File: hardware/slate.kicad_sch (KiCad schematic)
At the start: 0 parts

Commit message: DDR3 RAM symbol
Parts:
- added U1: A33, slate-lib:TFBGA-282_14x14mm_Layout17x17_P0.8mm, symbol slate-lib:A33
- added U2: H5TQ4G63EFR, Package_BGA:FBGA-96_7.5x13mm_Layout9x16_P0.8mm, symbol slate-lib:H5TQ4G63EFR
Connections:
- new net: U2.J1 (NC), U2.J9 (NC), U2.L1 (NC), U2.L9 (NC), U2.M7 (NC)
- new net GND: U1.F10 (GND), U1.F8 (GND), U1.F9 (GND), U1.G10 (GND), U1.G11 (GND), U1.G7 (GND), U1.G8 (GND), U1.G9 (GND), U1.H10 (GND), U1.H11 (GND), U1.H12 (GND), U1.H13 (AGND), U1.H7 (GND), U1.H8 (GND), U1.H9 (GND), U1.J10 (GND), U1.J11 (GND), U1.J12 (GND), U1.J7 (GND), U1.J8 (GND), U1.J9 (GND), U1.K10 (GND), U1.K11 (GND), U1.K12 (GND), U1.K7 (GND), U1.K8 (GND), U1.K9 (GND), U1.L10 (GND), U1.L11 (GND), U1.L8 (GND), U1.L9 (GND), U1.M10 (GND), U1.M9 (GND), U1.N4 (GND), U2.A9 (VSS), U2.B1 (VSSQ), U2.B3 (VSS), U2.B9 (VSSQ), U2.D1 (VSSQ), U2.D8 (VSSQ), U2.E1 (VSS), U2.E2 (VSSQ), U2.E8 (VSSQ), U2.F9 (VSSQ), U2.G1 (VSSQ), U2.G8 (VSS), U2.G9 (VSSQ), U2.J2 (VSS), U2.J8 (VSS), U2.M1 (VSS), U2.M9 (VSS), U2.P1 (VSS), U2.P9 (VSS), U2.T1 (VSS), U2.T9 (VSS)
- new net VCC-DRAM: U1.H5 (VCC-DRAM), U1.H6 (VCC-DRAM), U1.J5 (VCC-DRAM), U1.J6 (VCC-DRAM), U1.K5 (VCC-DRAM), U1.L5 (VCC-DRAM)
- new net VCC-IO: U1.E11 (VCC-IO), U1.E12 (VCC-IO), U1.F11 (VCC-IO), U1.F12 (VCC-IO), U1.G12 (VCC-IO)
- new net VCC-PD: U1.M11 (VCC-PD), U1.N11 (VCC-PD)
- new net VDD: U2.B2 (VDD), U2.D9 (VDD), U2.G7 (VDD), U2.K2 (VDD), U2.K8 (VDD), U2.N1 (VDD), U2.N9 (VDD), U2.R1 (VDD), U2.R9 (VDD)
- new net VDD-CPU: U1.E5 (VDD-CPU), U1.E6 (VDD-CPU), U1.E7 (VDD-CPU), U1.F5 (VDD-CPU), U1.F6 (VDD-CPU), U1.F7 (VDD-CPU), U1.G5 (VDD-CPU), U1.G6 (VDD-CPU)
- new net VDD-SYS: U1.E10 (VDD-SYS), U1.E8 (VDD-SYS), U1.E9 (VDD-SYS), U1.K6 (VDD-SYS), U1.L6 (VDD-SYS), U1.M6 (VDD-SYS), U1.M7 (VDD-SYS), U1.N10 (VDD-SYS), U1.N8 (VDD-SYS), U1.N9 (VDD-SYS)
- new net VDDQ: U2.A1 (VDDQ), U2.A8 (VDDQ), U2.C1 (VDDQ), U2.C9 (VDDQ), U2.D2 (VDDQ), U2.E9 (VDDQ), U2.F1 (VDDQ), U2.H2 (VDDQ), U2.H9 (VDDQ)

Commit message: Update
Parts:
- removed U1: A33, slate-lib:TFBGA-282_14x14mm_Layout17x17_P0.8mm, symbol slate-lib:A33
- removed U2: H5TQ4G63EFR, Package_BGA:FBGA-96_7.5x13mm_Layout9x16_P0.8mm, symbol slate-lib:H5TQ4G63EFR
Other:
- added sheet A33 (a33.kicad_sch)
- added sheet DDR3 RAM (ddr3.kicad_sch)
- added sheet Power (power.kicad_sch)
- note added: "An example A33 project"
- note added: "OSHWA A33 Computer"
- company: (none) -> Chengyin Yao (Cyao)
- title: (none) -> Slate

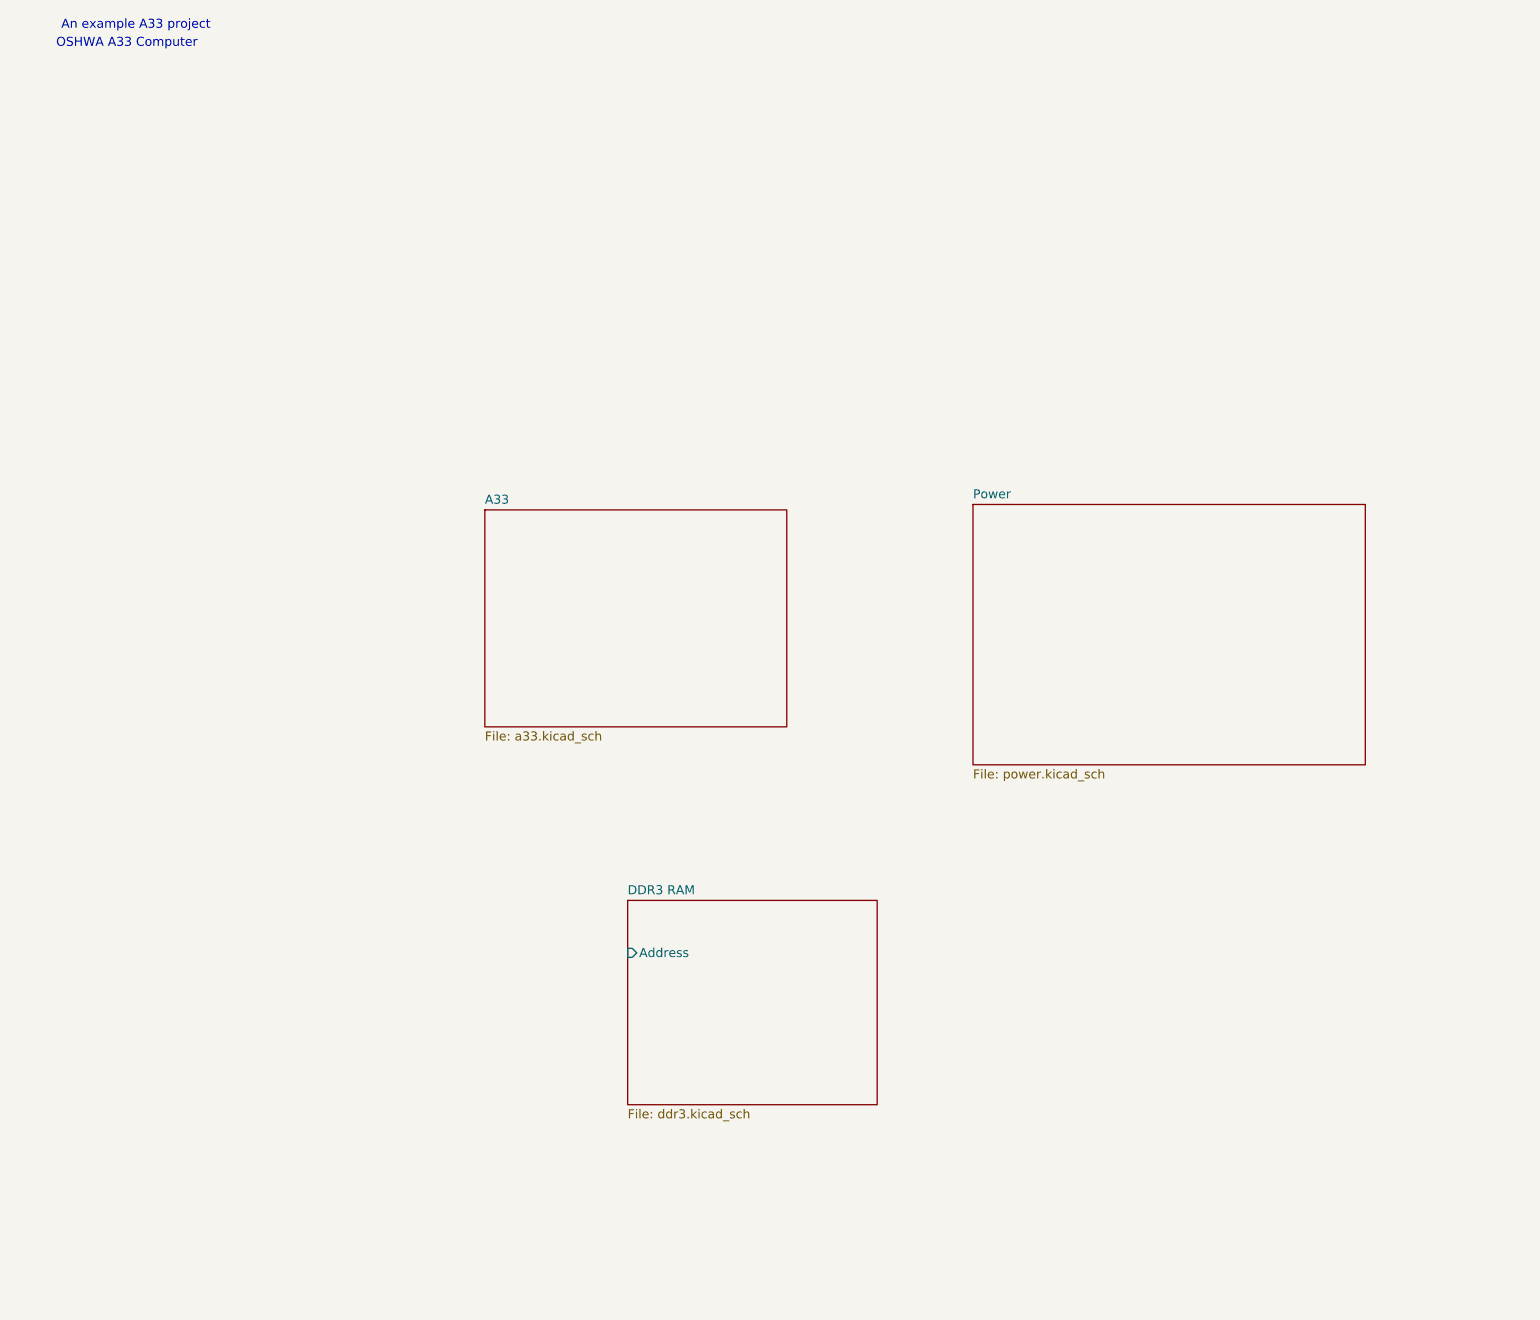
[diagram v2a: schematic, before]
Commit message: DDR3 schematic made
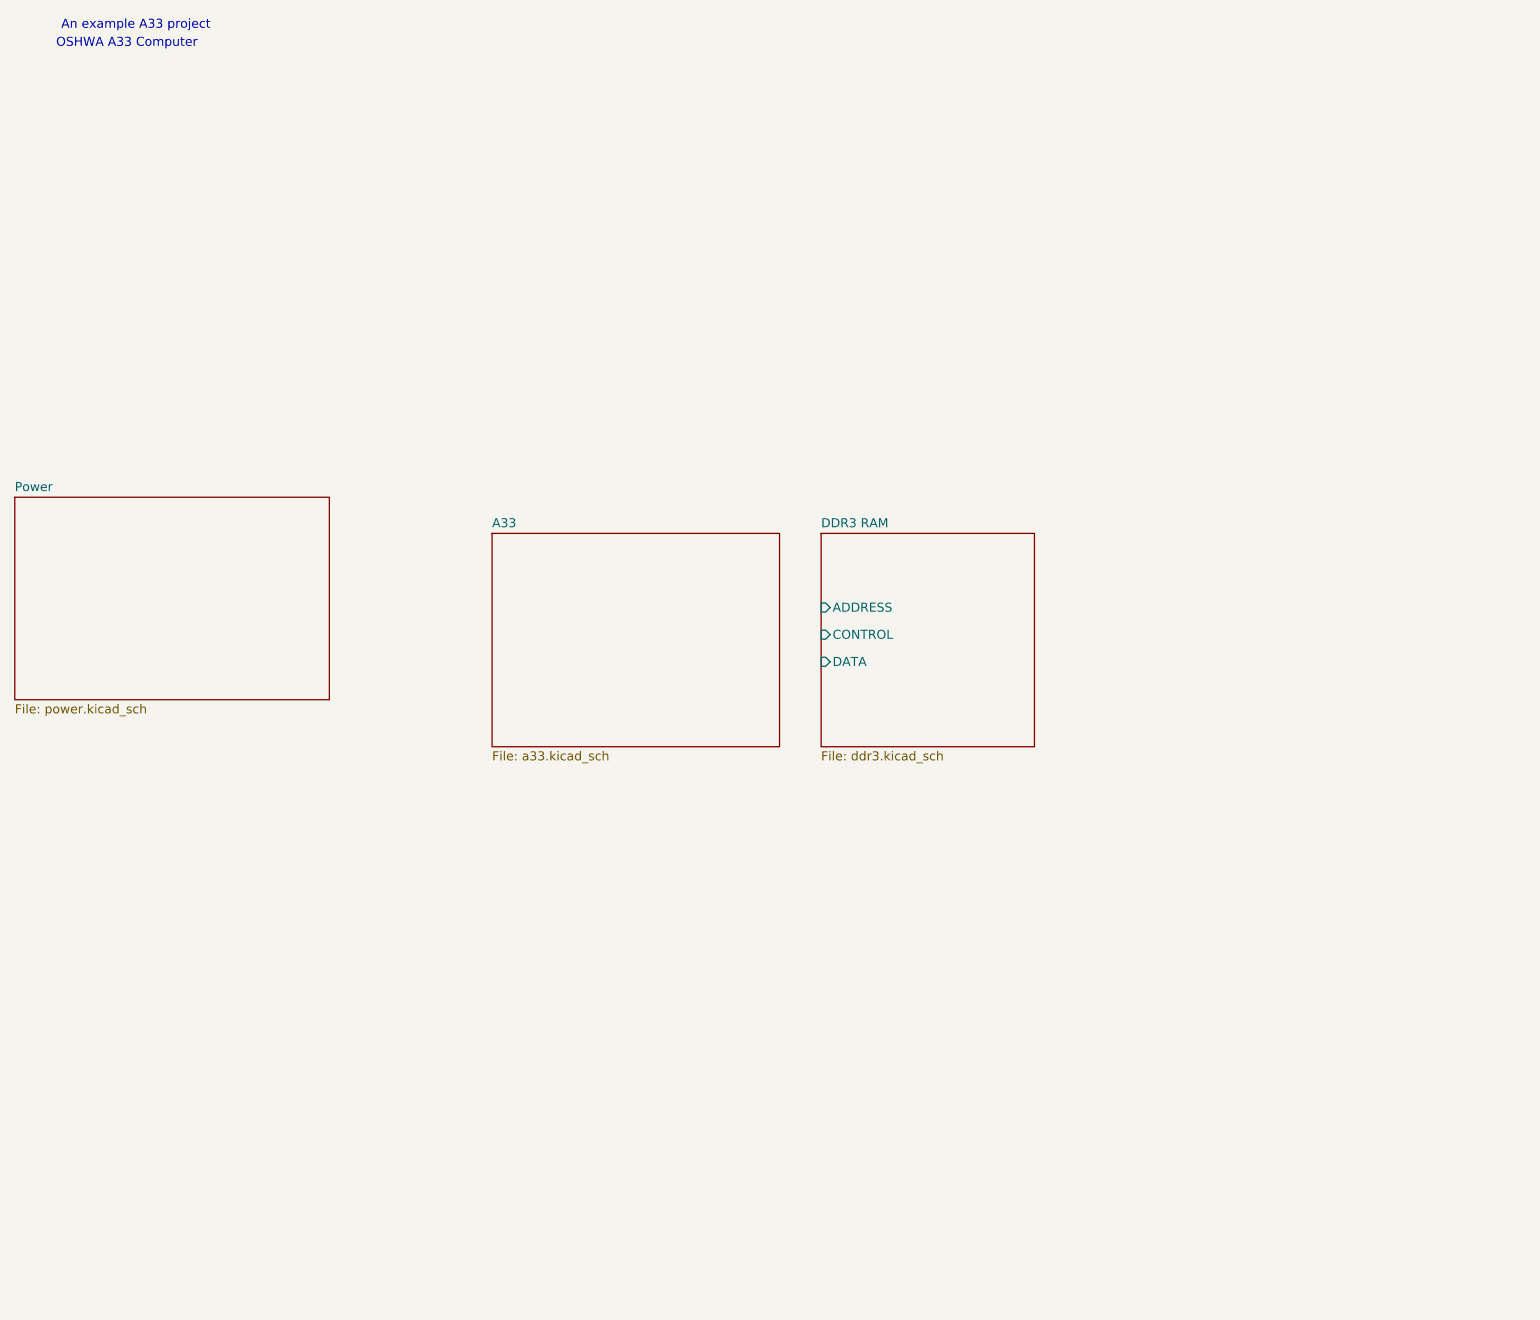
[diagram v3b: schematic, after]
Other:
- sheet DDR3 RAM ports: added ADDRESS, CONTROL, DATA; removed Address
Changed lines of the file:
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@@
 	)
 	(sheet
-		(at 93.98 137.414)
-		(size 35.052 28.702)
+		(at 121.158 85.852)
+		(size 29.972 29.972)
 		(exclude_from_sim no)
 		(in_bom yes)
@@
 		)
 		(property "Sheetname" "DDR3 RAM"
-			(at 93.98 136.7024 0)
+			(at 121.158 85.1404 0)
 			(effects
 				(font
@@
 		)
 		(property "Sheetfile" "ddr3.kicad_sch"
-			(at 93.98 166.7006 0)
+			(at 121.158 116.4086 0)
 			(effects
 				(font
@@
 			)
 		)
-		(pin "Address" input
-			(at 93.98 144.78 180)
+		(pin "ADDRESS" input
+			(at 121.158 96.266 180)
+			(effects
+				(font
+					(size 1.27 1.27)
+				)
+				(justify left)
+			)
+		)
+		(pin "CONTROL" input
+			(at 121.158 100.076 180)
+			(effects
+				(font
+					(size 1.27 1.27)
+				)
+				(justify left)
+			)
+		)
+		(pin "DATA" input
+			(at 121.158 103.886 180)
 			(effects
 				(font
@@
 	)
 	(sheet
-		(at 73.914 82.55)
-		(size 42.418 30.48)
+		(at 74.93 85.852)
+		(size 40.386 29.972)
 		(exclude_from_sim no)
 		(in_bom yes)
@@
 		)
 		(property "Sheetname" "A33"
-			(at 73.914 81.8384 0)
+			(at 74.93 85.1404 0)
 			(effects
 				(font
@@
 		)
 		(property "Sheetfile" "a33.kicad_sch"
-			(at 73.914 113.6146 0)
+			(at 74.93 116.4086 0)
 			(effects
 				(font
@@
 	)
 	(sheet
-		(at 142.494 81.788)
-		(size 55.118 36.576)
+		(at 7.874 80.772)
+		(size 44.196 28.448)
 		(exclude_from_sim no)
 		(in_bom yes)
@@
 		)
 		(property "Sheetname" "Power"
-			(at 142.494 81.0764 0)
+			(at 7.874 80.0604 0)
 			(effects
 				(font
@@
 		)
 		(property "Sheetfile" "power.kicad_sch"
-			(at 142.494 118.9486 0)
+			(at 7.874 109.8046 0)
 			(effects
 				(font

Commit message: Update
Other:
- sheet A33 ports: added A[0..15], D[0..15], {DDR_CONTROL}; removed none
- sheet DDR3 RAM ports: added A[0..15], D[0..15], {DDR_CONTROL}; removed ADDRESS, CONTROL, DATA
- note added: "Project Volatile Schematic"
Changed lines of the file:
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@@
+		)
+	)
+	(text "Project Volatile Schematic"
+		(exclude_from_sim no)
+		(at 26.162 19.304 0)
+		(effects
+			(font
+				(size 1.27 1.27)
+			)
+			(href "https://www.eevblog.com/forum/projects/jlc2313-stackup-with-ddr3-fly-by/?action=dlattach;attach=990376")
 		)
 	)
@@
 		)
 	)
+	(bus
+		(pts
+			(xy 142.24 106.68) (xy 148.59 106.68)
+		)
+		(stroke
+			(width 0)
+			(type default)
+		)
+	)
+	(bus
+		(pts
+			(xy 142.24 102.87) (xy 148.59 102.87)
+		)
+		(stroke
+			(width 0)
+			(type default)
+		)
+	)
+	(bus
+		(pts
+			(xy 142.24 110.49) (xy 148.59 110.49)
+		)
+		(stroke
+			(width 0)
+			(type default)
+		)
+	)
 	(sheet
-		(at 121.158 85.852)
-		(size 29.972 29.972)
+		(at 148.59 93.218)
+		(size 29.718 28.194)
 		(exclude_from_sim no)
 		(in_bom yes)
@@
 		)
 		(property "Sheetname" "DDR3 RAM"
-			(at 121.158 85.1404 0)
+			(at 148.59 92.5064 0)
 			(effects
 				(font
@@
 		)
 		(property "Sheetfile" "ddr3.kicad_sch"
-			(at 121.158 116.4086 0)
+			(at 148.59 121.9966 0)
 			(effects
 				(font
@@
 			)
 		)
-		(pin "ADDRESS" input
-			(at 121.158 96.266 180)
+		(pin "A[0..15]" input
+			(at 148.59 102.87 180)
 			(effects
 				(font
@@
 			)
 		)
-		(pin "CONTROL" input
-			(at 121.158 100.076 180)
+		(pin "D[0..15]" bidirectional
+			(at 148.59 106.68 180)
 			(effects
 				(font
@@
 			)
 		)
-		(pin "DATA" input
-			(at 121.158 103.886 180)
+		(pin "{DDR_CONTROL}" bidirectional
+			(at 148.59 110.49 180)
 			(effects
 				(font
@@
 	)
 	(sheet
-		(at 74.93 85.852)
-		(size 40.386 29.972)
+		(at 106.68 93.218)
+		(size 35.56 28.194)
 		(exclude_from_sim no)
 		(in_bom yes)
@@
 		)
 		(property "Sheetname" "A33"
-			(at 74.93 85.1404 0)
+			(at 106.68 92.5064 0)
 			(effects
 				(font
@@
 		)
 		(property "Sheetfile" "a33.kicad_sch"
-			(at 74.93 116.4086 0)
+			(at 106.68 121.9966 0)
 			(effects
 				(font
@@
 				)
 				(justify left top)
+			)
+		)
+		(pin "A[0..15]" output
+			(at 142.24 102.87 0)
+			(effects
+				(font
+					(size 1.27 1.27)
+				)
+				(justify right)
+			)
+		)
+		(pin "D[0..15]" bidirectional
+			(at 142.24 106.68 0)
+			(effects
+				(font
+					(size 1.27 1.27)
+				)
+				(justify right)
+			)
+		)
+		(pin "{DDR_CONTROL}" bidirectional
+			(at 142.24 110.49 0)
+			(effects
+				(font
+					(size 1.27 1.27)
+				)
+				(justify right)
 			)
 		)
@@
 	)
 	(sheet
-		(at 7.874 80.772)
-		(size 44.196 28.448)
+		(at 58.674 93.218)
+		(size 33.528 28.194)
 		(exclude_from_sim no)
 		(in_bom yes)
@@
 		)
 		(property "Sheetname" "Power"
-			(at 7.874 80.0604 0)
+			(at 58.674 92.5064 0)
 			(effects
 				(font
@@
 		)
 		(property "Sheetfile" "power.kicad_sch"
-			(at 7.874 109.8046 0)
-			(effects
-				(font
+			(at 58.674 121.9966 0)
+			(effects
+				(font

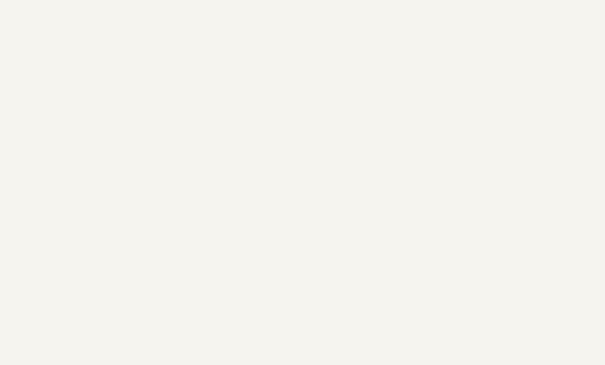
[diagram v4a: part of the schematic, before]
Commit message: Start of psu
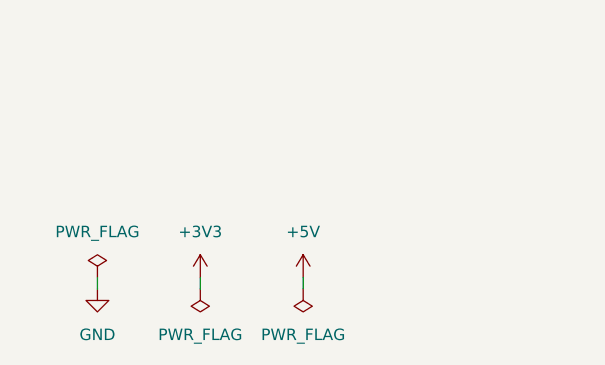
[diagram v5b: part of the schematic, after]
